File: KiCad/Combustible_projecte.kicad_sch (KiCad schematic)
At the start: 0 parts

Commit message: dibuix micro creat
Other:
- added sheet Micro (Micro.kicad_sch)
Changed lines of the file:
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@@
 	(generator_version "9.0")
 	(paper "A4")
+	(sheet
+		(at 129.54 34.29)
+		(size 48.26 30.48)
+		(exclude_from_sim no)
+		(in_bom yes)
+		(on_board yes)
+		(dnp no)
+		(fields_autoplaced yes)
+		(stroke
+			(width 0.1524)
+			(type solid)
+		)
+		(fill
+			(color 0 0 0 0.0000)
+		)
+		(property "Sheetname" "Micro"
+			(at 129.54 33.5784 0)
+			(effects
+				(font
+					(size 1.27 1.27)
+				)
+				(justify left bottom)
+			)
+		)
+		(property "Sheetfile" "Micro.kicad_sch"
+			(at 129.54 65.3546 0)
+			(effects
+				(font
+					(size 1.27 1.27)
+				)
+				(justify left top)
+			)
+		)
+		(instances
+			(project "Combustible_projecte"
+				(path "/c989196d-f442-462e-ad13-2ff17993bc1b"
+					(page "2")
+				)
+			)
+		)
+	)
 	(sheet_instances
 		(path "/"

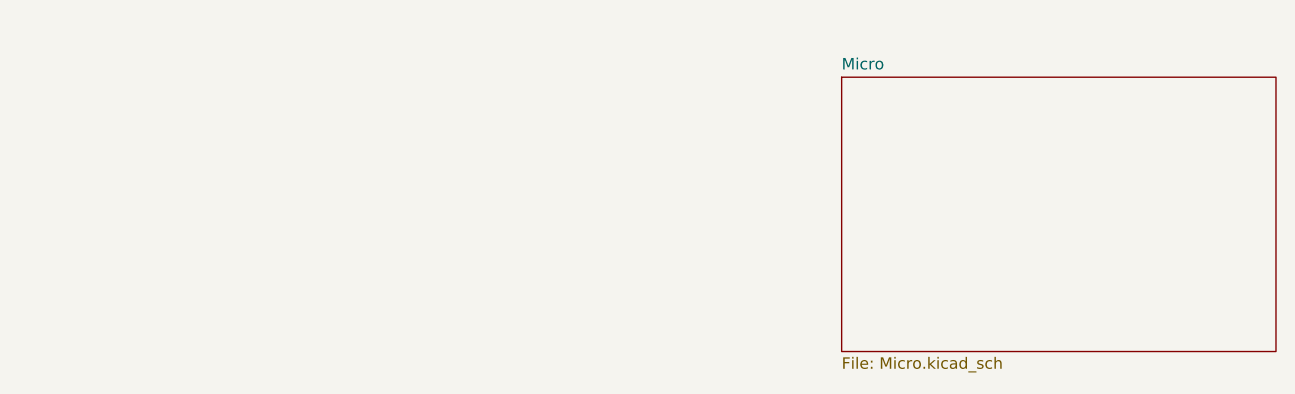
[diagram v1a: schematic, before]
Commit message: Afegit el micro i les etapes del bus CAN i USART, també afegit el cristall i el debug
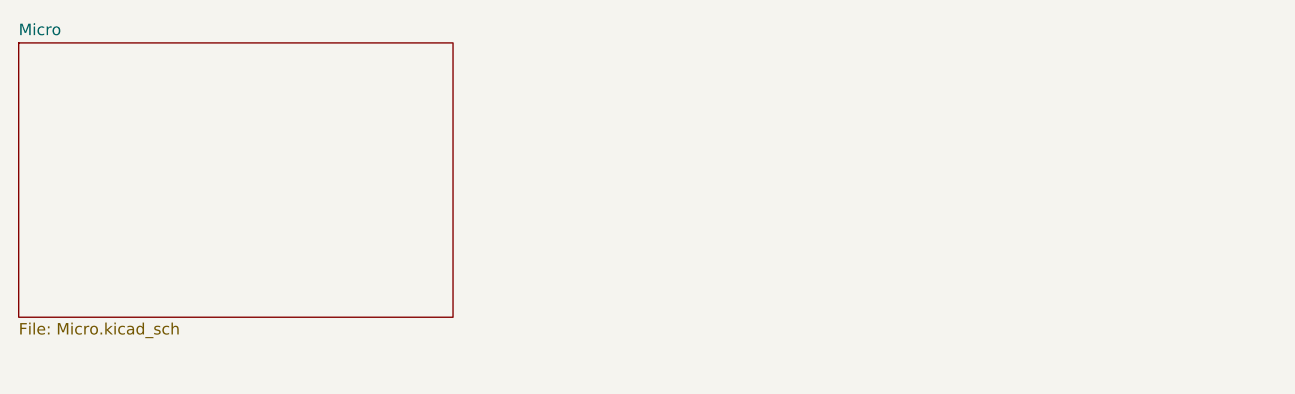
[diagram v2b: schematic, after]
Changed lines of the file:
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@@
 	(paper "A4")
 	(sheet
-		(at 129.54 34.29)
+		(at 38.1 30.48)
 		(size 48.26 30.48)
 		(exclude_from_sim no)
@@
 		)
 		(property "Sheetname" "Micro"
-			(at 129.54 33.5784 0)
+			(at 38.1 29.7684 0)
 			(effects
 				(font
@@
 		)
 		(property "Sheetfile" "Micro.kicad_sch"
-			(at 129.54 65.3546 0)
+			(at 38.1 61.5446 0)
 			(effects
 				(font
